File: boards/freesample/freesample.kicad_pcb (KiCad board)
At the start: 8 copper layers, 576 parts, among them J1 SMA, J10 XILINX_JTAG, J11 SMA, J12 SMA, J13 SMA, J14 SMA, J15 SMA, J16 SMA, J17 SMA, J18 SMA, J19 JUMPER, J2 BARREL, J20 JUMPER, J21 JUMPER, J22 SMA, J23 SMA, J24 SMA, J25 SMA, J26 PMOD_HOST, J3 SMA, J4 SMA, J5 SMA, J6 XILINX_JTAG, J7 CONN_INTEGRALSTICK_FPGA_HOST, J8 CONN_INTEGRALSTICK_MCU_HOST, J9 0826-1G1T-23-F, M1 TRACEPAD, M2 LOGO1, M3 LOGO2, M4 LOGO3, M5 LOGO4, M6 LOGO5, M7 LOGO6, Q1 SSM6N58NU, U1 HMC675LP3E, U10 PI6C59S6005, U11 PI6C59S6005, U12 PI6C59S6005, U13 SIP32408, U14 LMK04806, U15 ASG-D-V-A-125.000MHZ, U16 HMC856, U17 NB6L295, U18 PI6C59S6005, U19 NB7V52MMNG, U2 HMC675LP3E, U20 NB7V52MMNG, U21 NB7V52MMNG, U22 PI6C59S6005, U26 MCP1755ST-5002E/MC, U27 LM27761, U28 ADP1763Z-1.0, U29 ADP1763Z-1.0, U3 PI6C59S6005, U30 OKL-T/3-W12P-C, U31 ADP1741, U32 OKL-T/3-W12P-C, U33 ADP1741, U34 ADP1741, U35 OKL-T/3-W12P-C, U36 OKL-T/3-W12P-C, U37 LM27761, U38 OKL-T/3-W12P-C, U39 LM27761, U4 LTC2664CUH-16#PBF, U40 DS25BR150, U41 DS25BR150, U42 ADP1741, U43 ADP1741, U5 TLK10232, U6 LMK61PD0A2, U7 PI6C59S6005, U8 HMC675LP3E, U9 HMC675LP3E

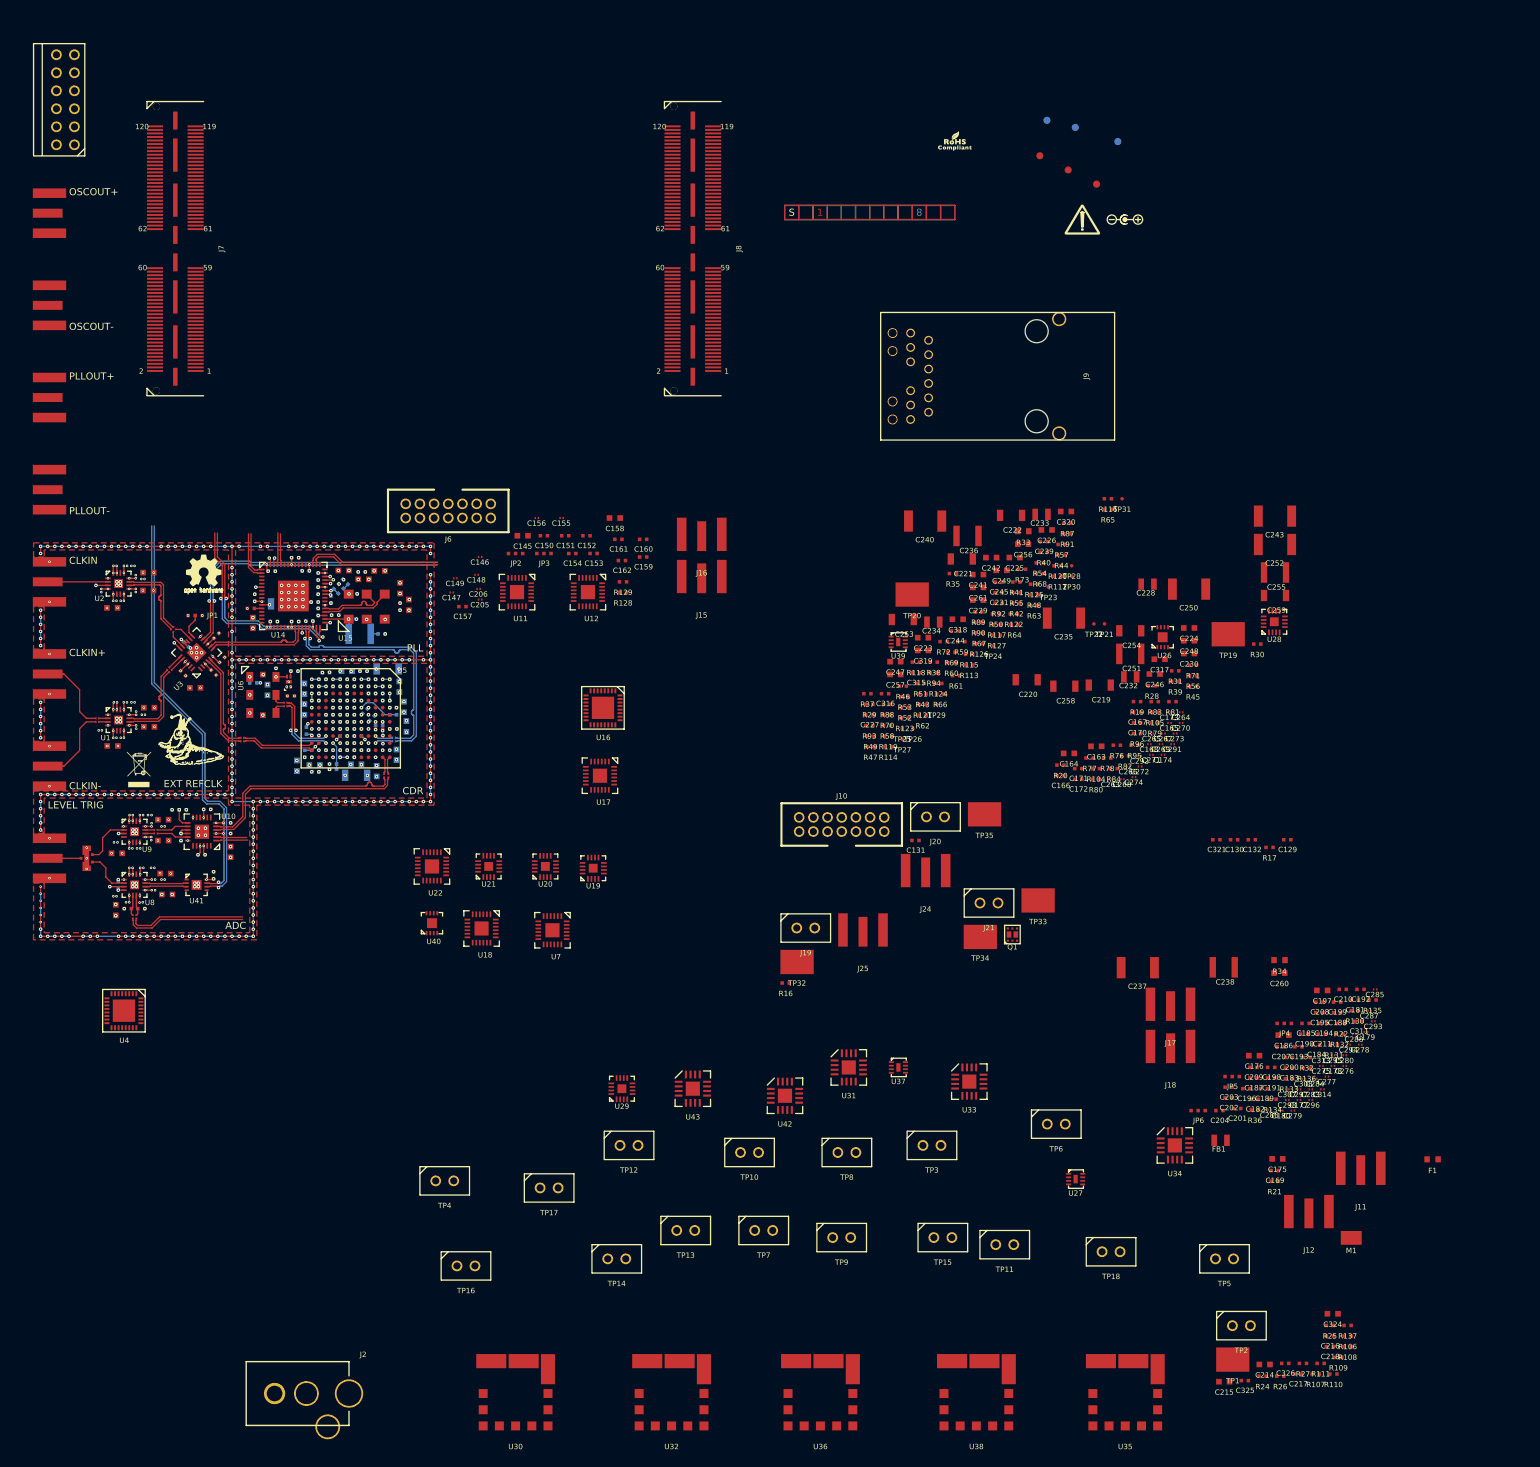
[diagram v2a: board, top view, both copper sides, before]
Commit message: Continued layout on clock muxing
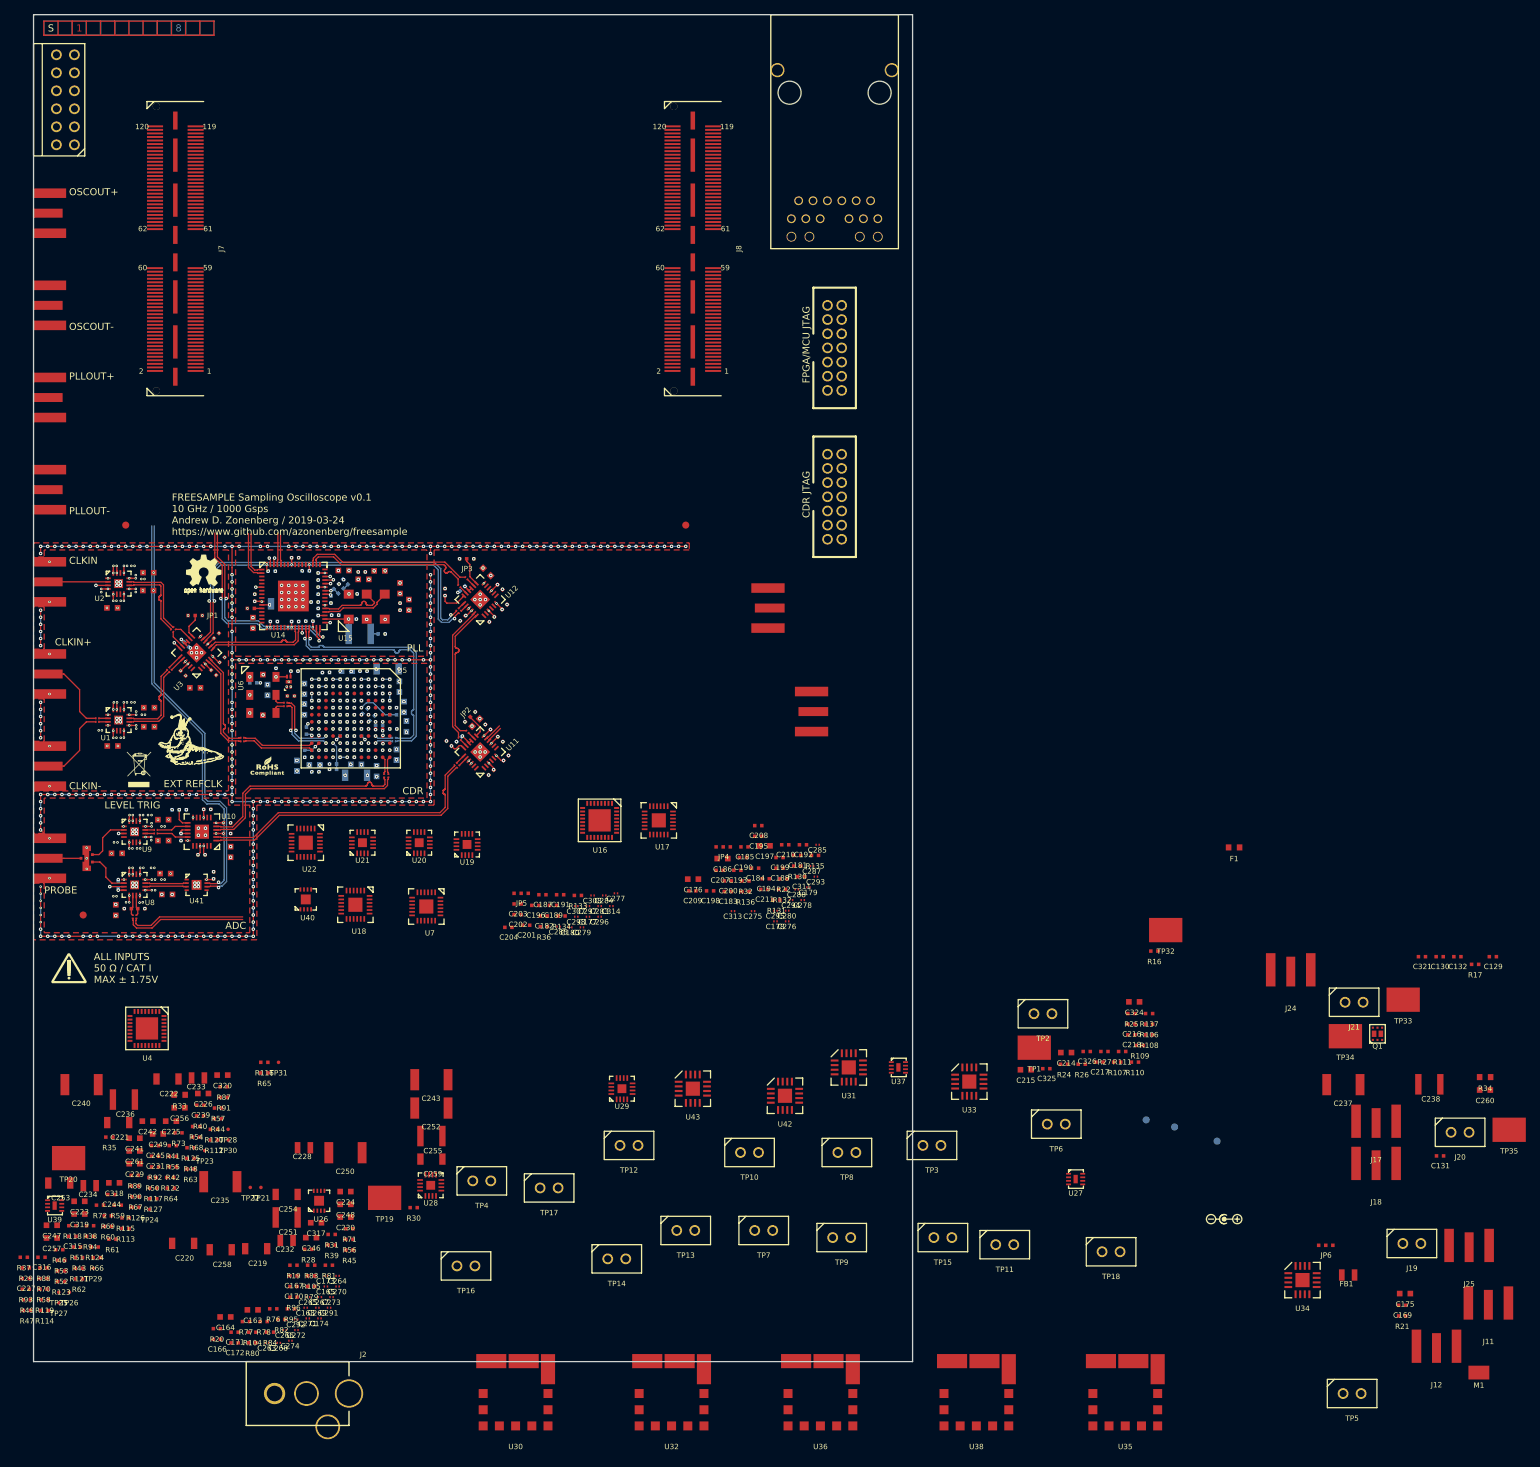
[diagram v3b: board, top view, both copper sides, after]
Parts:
- C154, C157: moved to B.Cu
- moved M6 177.7 mm to (21.0, 179.5)
- moved FID4 174.2 mm to (23.0, 172.0)
- moved FID3 145.2 mm to (29.0, 117.0)
- moved C221 143.1 mm to (27.9, 201.3)
- moved C225 143.1 mm to (35.4, 201.1)
- moved C228 143.1 mm to (54.1, 204.8)
- moved C229 143.1 mm to (30.2, 207.1)
- moved C236 143.1 mm to (28.7, 198.0)
- moved C239 143.1 mm to (39.5, 198.8)
- moved C242 143.1 mm to (32.1, 201.1)
- moved C320 143.1 mm to (42.6, 194.6)
- moved R125 143.1 mm to (38.1, 204.8)
- moved R35 143.1 mm to (26.7, 203.3)
- moved R40 143.1 mm to (39.5, 200.3)
- moved R48 143.1 mm to (38.1, 206.3)
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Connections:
- C148 pad 1: /Sample clock muxing/EXT_CLK_AC_P -> /Sample clock muxing/MUXCLK0_AC_P
- C148 pad 2: /Sample clock muxing/EXT_SAMPCLK_P -> /Sample clock muxing/MUXCLK0_P
- C149 pad 1: /Sample clock muxing/EXT_CLK_AC_N -> /Sample clock muxing/MUXCLK0_AC_N
- C149 pad 2: /Sample clock muxing/EXT_SAMPCLK_N -> /Sample clock muxing/MUXCLK0_N
- C155 pad 1: /Sample clock muxing/MUXCLK0_AC_P -> /Sample clock muxing/MUXCLK1_AC_N
- C155 pad 2: /Sample clock muxing/MUXCLK0_P -> /Sample clock muxing/EXT_SAMPCLK_N
- C156 pad 1: /Sample clock muxing/MUXCLK0_AC_N -> /Sample clock muxing/MUXCLK1_AC_P
- C156 pad 2: /Sample clock muxing/MUXCLK0_N -> /Sample clock muxing/EXT_SAMPCLK_P
- C205 pad 1: /Sample clock muxing/MUXCLK1_AC_P -> /Sample clock muxing/EXT_CLK_AC_N
- C205 pad 2: /Sample clock muxing/PLL_SAMPCLK_P -> /Sample clock muxing/PLL_SAMPCLK_N
- C206 pad 1: /Sample clock muxing/MUXCLK1_AC_N -> /Sample clock muxing/EXT_CLK_AC_P
- C206 pad 2: /Sample clock muxing/PLL_SAMPCLK_N -> /Sample clock muxing/PLL_SAMPCLK_P
- J15 pad 1: /Sample clock muxing/CLKOUT2_P -> /Sample clock muxing/CLKOUT2_N
- J16 pad 1: /Sample clock muxing/CLKOUT2_N -> /Sample clock muxing/CLKOUT2_P
- U11 pad 10: (no net) -> /Sample clock muxing/CLKOUT2_N
- U11 pad 11: (no net) -> /Sample clock muxing/CLKOUT2_P
- U11 pad 14: /Sample clock muxing/LVL_CLK_AC_N -> /Sample clock muxing/MUXCLK0_AC_P
- U11 pad 17: /Sample clock muxing/LVL_CLK_AC_P -> /Sample clock muxing/MUXCLK0_AC_N
- U11 pad 18: /SAMP_MUXSEL0 -> /SAMP_MUXSEL1
- U11 pad 19: /Sample clock muxing/EXT_CLK_AC_N -> /Sample clock muxing/LVL_CLK_AC_P
- U11 pad 20: /Sample clock muxing/EXT_CLK_AC_P -> /Sample clock muxing/LVL_CLK_AC_N
- U11 pad 23: /Sample clock muxing/MUXCLK0_P -> /Phase control/CLKIN0_N
- U11 pad 24: /Sample clock muxing/MUXCLK0_N -> /Phase control/CLKIN0_P
- U11 pad 4: (no net) -> /Phase control/CLKIN1_N
- U11 pad 5: (no net) -> /Phase control/CLKIN1_P
- U12 pad 1: /Phase control/CLKIN1_P -> (no net)
- U12 pad 14: /Sample clock muxing/MUXCLK0_AC_N -> /Sample clock muxing/EXT_CLK_AC_P
- U12 pad 17: /Sample clock muxing/MUXCLK0_AC_P -> /Sample clock muxing/EXT_CLK_AC_N
- U12 pad 18: /SAMP_MUXSEL1 -> /SAMP_MUXSEL0
- U12 pad 19: /Sample clock muxing/MUXCLK1_AC_N -> /Sample clock muxing/MUXCLK1_AC_P
- U12 pad 2: /Phase control/CLKIN1_N -> (no net)
- U12 pad 20: /Sample clock muxing/MUXCLK1_AC_P -> /Sample clock muxing/MUXCLK1_AC_N
- U12 pad 23: /Phase control/CLKIN0_P -> /Sample clock muxing/MUXCLK0_N
- U12 pad 24: /Phase control/CLKIN0_N -> /Sample clock muxing/MUXCLK0_P
- U12 pad 4: /Sample clock muxing/CLKOUT2_P -> (no net)
- U12 pad 5: /Sample clock muxing/CLKOUT2_N -> (no net)
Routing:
- net /3V3_CLKBUF: track 90.6 -> 201.1 mm, vias 23 -> 47
- net /GND: track 764.2 -> 855.8 mm, vias 481 -> 541
- net /Level triggering/LTRIG_SAMPOUT_P: track 4.35 -> 40.9 mm
- net /Level triggering/LTRIG_SAMPOUT_N: track 4.50 -> 40.9 mm
- net /SAMP_MUXSEL1: track 0.00 -> 34.0 mm, vias 0 -> 1
- net /Sample clock muxing/MUXCLK0_P: track 0.00 -> 19.2 mm
- net /Sample clock muxing/MUXCLK0_N: track 0.00 -> 19.1 mm
- net /SAMP_MUXSEL0: track 0.00 -> 13.3 mm, vias 0 -> 1
- net /Sample clock muxing/EXT_SAMPCLK_N: track 42.6 -> 53.6 mm, vias 1 -> 2
- net /Sample clock muxing/EXT_SAMPCLK_P: track 42.9 -> 53.6 mm, vias 1 -> 2
- net /Sample clock muxing/PLL_SAMPCLK_N: track 18.5 -> 23.9 mm
- net /Sample clock muxing/PLL_SAMPCLK_P: track 19.1 -> 23.9 mm
- net /Sample clock muxing/BUF3_IN_SEL: track 0.00 -> 4.02 mm
- net /Sample clock muxing/BUF2_IN_SEL: track 0.00 -> 3.26 mm
- net /Sample clock muxing/CLKOUT2_P: track 0.00 -> 2.55 mm
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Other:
- board outline added: 124 x 190 mm
- board text added: "ALL INPUTS 50 Ω / CAT I MAX ± 1.75V"
- board text added: "CDR JTAG"
- board text added: "FPGA/MCU JTAG"
- board text added: "FREESAMPLE Sampling Oscilloscope v0.1 10 GHz / 1000 Gsps Andrew D. Zonenberg / 2019-03-24 https://www.github.com/azonenberg/freesample"
- board text added: "PROBE"

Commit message: Initial layout of coarse delay line
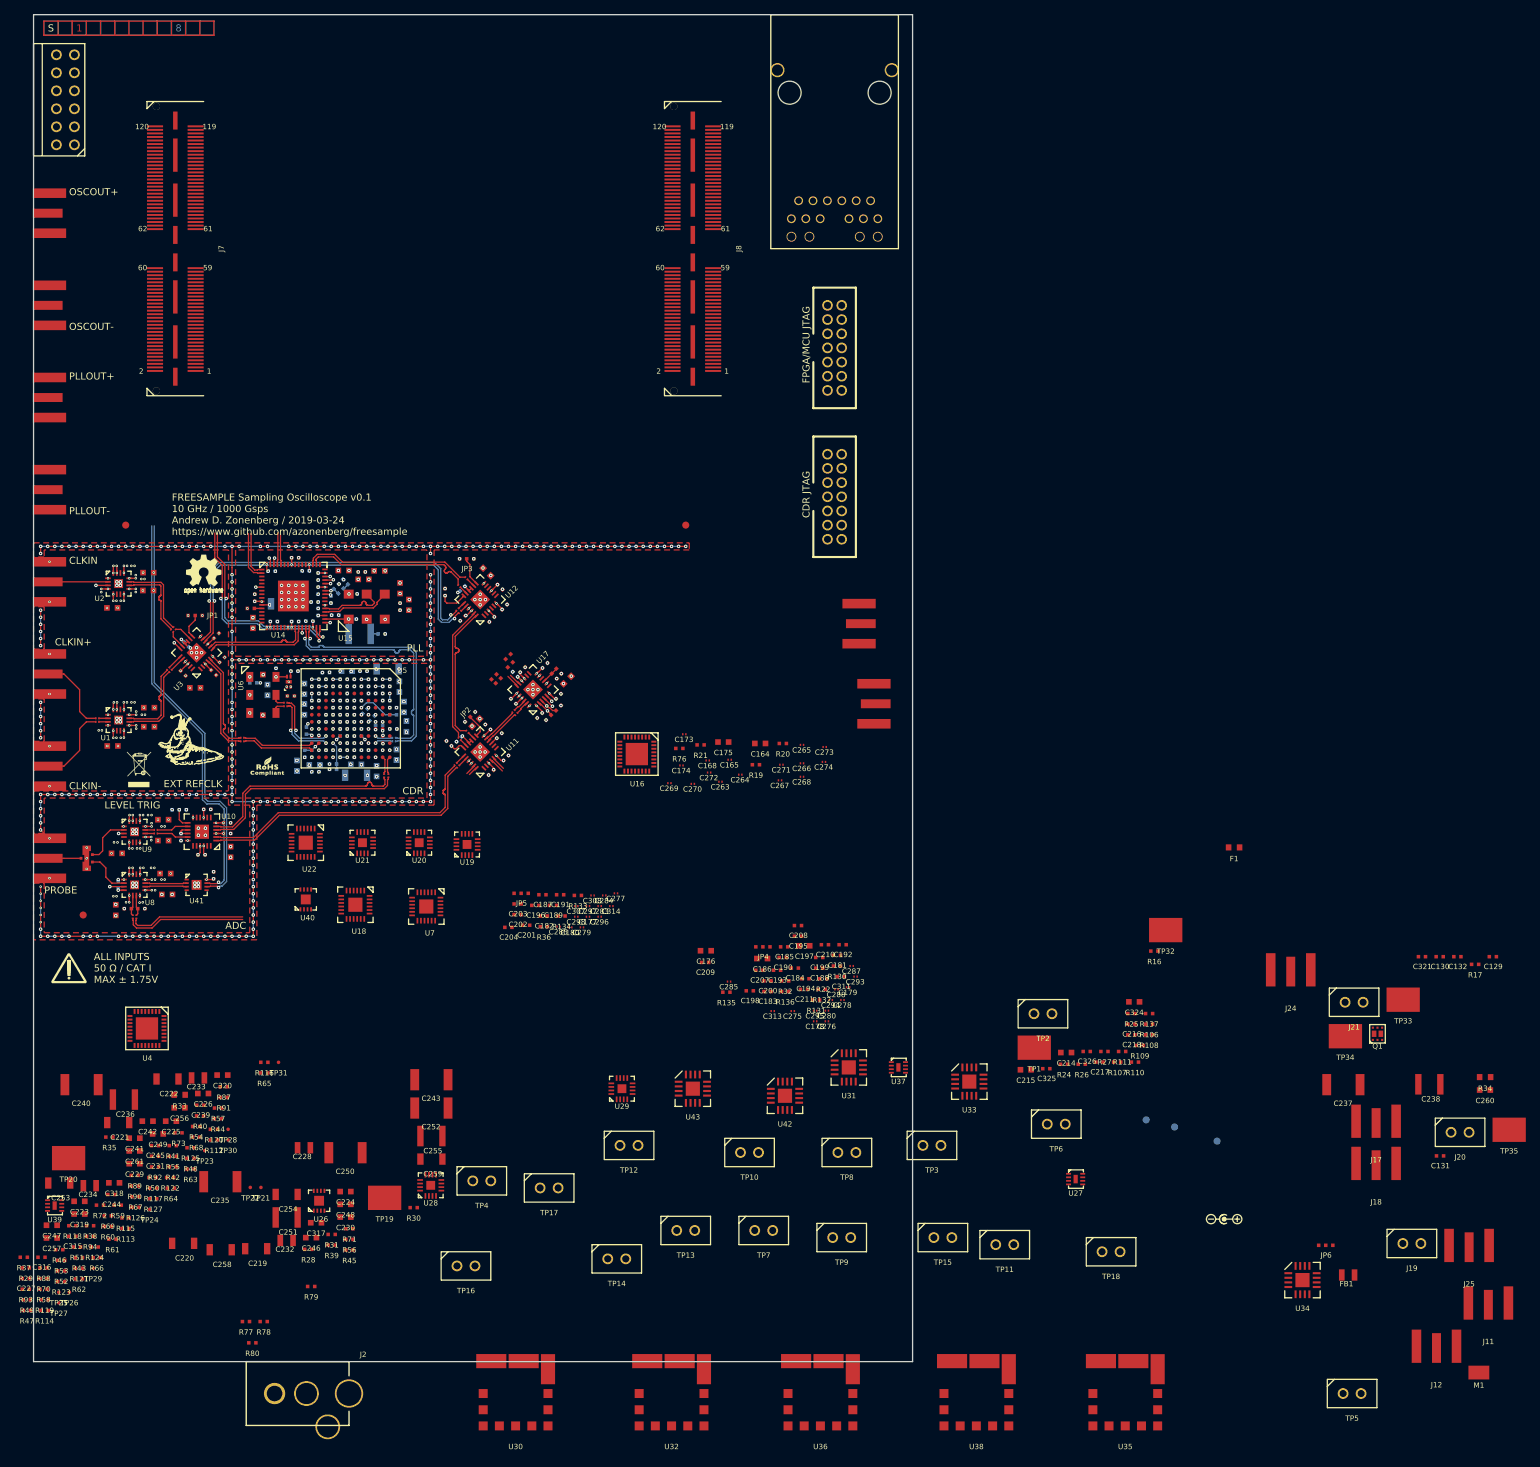
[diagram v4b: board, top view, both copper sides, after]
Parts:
- C171: moved to B.Cu
- moved C169 153.1 mm to (85.0, 137.4), turned to 45 degrees
- moved R21 127.6 mm to (110.1, 148.0)
- moved C175 123.7 mm to (113.3, 147.6)
- moved R20 114.8 mm to (121.7, 147.8)
- moved C274 111.0 mm to (127.5, 150.4)
- moved C164 110.6 mm to (118.5, 147.8)
- moved C268 108.7 mm to (124.4, 152.5)
- moved C266 108.2 mm to (124.4, 150.6)
- moved C166 105.7 mm to (88.2, 136.8), turned to 45 degrees
- moved C265 104.5 mm to (124.4, 148.0)
- moved C273 104.2 mm to (127.6, 148.3)
- moved C271 102.8 mm to (121.5, 150.8)
- moved C263 101.8 mm to (112.9, 153.2)
- moved C171 100.9 mm to (84.0, 138.1), turned to 135 degrees
- moved R84 100.1 mm to (83.2, 136.7), turned to 45 degrees
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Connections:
- U11 pad 10: /Sample clock muxing/CLKOUT2_N -> /Phase control/CLKIN1_N
- U11 pad 11: /Sample clock muxing/CLKOUT2_P -> /Phase control/CLKIN1_P
- U11 pad 4: /Phase control/CLKIN1_N -> (no net)
- U11 pad 5: /Phase control/CLKIN1_P -> (no net)
- U11 pad 7: (no net) -> /Sample clock muxing/CLKOUT2_N
- U11 pad 8: (no net) -> /Sample clock muxing/CLKOUT2_P
- U17 pad 17: /Phase control/COARSEPHASE_N -> /Phase control/COARSEPHASE_P
- U17 pad 18: /Phase control/COARSEPHASE_P -> /Phase control/COARSEPHASE_N
- U17 pad 22: /Phase control/CLKIN1_AC_N -> /Phase control/CLKIN1_AC_P
- U17 pad 23: /Phase control/CLKIN1_AC_P -> /Phase control/CLKIN1_AC_N
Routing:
- net /GND: track 855.8 -> 909.2 mm, vias 541 -> 560
- net /COARSE_EN: track 0.00 -> 32.1 mm, vias 0 -> 1
- net /3V3: track 96.4 -> 127.9 mm, vias 30 -> 45
- net /COARSE_SLOAD: track 0.00 -> 30.8 mm, vias 0 -> 1
- net /COARSE_SDIN: track 0.00 -> 28.6 mm, vias 0 -> 1
- net /COARSE_SCLK: track 0.00 -> 26.9 mm, vias 0 -> 1
- net /Phase control/CLKIN1_P: track 0.00 -> 5.26 mm
- net /Phase control/CLKIN1_N: track 0.00 -> 5.26 mm
- net (no net): track 0.00 -> 4.13 mm
- net /Sample clock muxing/CLKOUT2_P: track 2.55 -> 0.00 mm
- net Net-(R81-Pad1): track 0.00 -> 2.45 mm
- net /Sample clock muxing/CLKOUT2_N: track 2.40 -> 0.00 mm
- net /Phase control/CLKIN1_AC_N: track 0.00 -> 2.04 mm
- net /Phase control/CLKIN1_AC_P: track 0.00 -> 1.95 mm
- net /Phase control/COARSEPHASE_N: track 0.00 -> 1.84 mm
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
